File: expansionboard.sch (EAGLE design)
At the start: 40 parts, among them IC2 REG1117, IC3 REG1117, U1 LAN951X, X1 J1012F21R, Y1 20Mhz

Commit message: for now, a complete logic board and expansion board until I find something wrong with it
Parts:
- added C12, C13: (no value), SparkFun-Capacitors:CAPEZ
- added C14, C15, C19, C20: 0.1uf, SparkFun-Capacitors:CAP1206
- added C18: 4.7uf, SparkFun-Capacitors:CAP1206
- added JP1: USB-A-S, SparkFun-Connectors:USB-A-S
- added R8: (no value), SparkFun-Resistors:RESISTOR1206
- added R9: 0ohm, SparkFun-Resistors:RESISTOR1206
- added X2, X3, X4: PCI-60-POS-145167, con-amp:PCI-60-POS-145167
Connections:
- removed net 3.3V_AN: R1.2, R2.2, R3.2, R4.2
- new net N$27: U1_USB0.CLK24_OUT
- new net USB2+: U1_USB0.USB_DP2_P, X2-1.1, X2-2.1
- new net USB2-: U1_USB0.USB_DM2_N, X2-3.1, X2-4.1
- new net USB2_PWR: U1_USB0.PRTCTRL2, X2-5.1, X2-6.1
- new net USB3+: U1_USB0.USB_DP3_P, X3-1.1, X3-2.1
- new net USB3-: U1_USB0.USB_DM3_N, X3-3.1, X3-4.1
- new net USB3_PWR: U1_USB0.PRTCTRL3, X3-5.1, X3-6.1
- new net USB4+: U1_USB1.USB_DP4_P, X4-1.1, X4-2.1
- new net USB4-: U1_USB1.USB_DM4_N, X4-3.1, X4-4.1
- new net USB4_PWR: U1_USB1.PRTCTRL4, X4-5.1, X4-6.1
- new net USB5+: JP1.D+, U1_USB1.USB_DP5_P
- new net USB5-: JP1.D-, U1_USB1.USB_DM5_N
- new net USB5_PWR: JP1.VBUS, U1_USB1.PRTCTRL5
- new net VBUS_DET: R8.1, U1_USB0.VBUS_DET
- new net VDD18CORE: C18.1, C19.1, C20.1, U1_PWR.VDD_1V8_CORE1, U1_PWR.VDD_1V8_CORE2
- new net VDDA33: C14.1, C15.1, R1.2, R2.2, R3.2, R4.2, R9.2
- net 3.3V: now also C12.1, C13.1, R8.2, R9.1, U1_PWR.VDD_3V3_A1, U1_PWR.VDD_3V3_A2, U1_PWR.VDD_3V3_A3, U1_PWR.VDD_3V3_A4, U1_PWR.VDD_3V3_A5, U1_PWR.VDD_3V3_A6, U1_PWR.VDD_3V3_A7, U1_PWR.VDD_3V3_IO1, U1_PWR.VDD_3V3_IO2, U1_PWR.VDD_3V3_IO3, U1_PWR.VDD_3V3_IO4, U1_PWR.VDD_3V3_IO5
- net 5V: now also X2-13.1, X2-14.1, X2-15.1, X2-16.1, X2-17.1, X2-18.1, X3-13.1, X3-14.1, X3-15.1, X3-16.1, X3-17.1, X3-18.1, X4-13.1, X4-14.1, X4-15.1, X4-16.1, X4-17.1, X4-18.1
- net GND: now also C12.2, C13.2, C14.2, C15.2, C18.2, C19.2, C20.2, JP1.GND, X2-10.1, X2-11.1, X2-115.1, X2-116.1, X2-117.1, X2-118.1, X2-119.1, X2-12.1, X2-120.1, X2-7.1, X2-8.1, X2-9.1, X3-10.1, X3-11.1, X3-115.1, X3-116.1, X3-117.1, X3-118.1, X3-119.1, X3-12.1, X3-120.1, X3-7.1, X3-8.1, X3-9.1, X4-10.1, X4-11.1, X4-115.1, X4-116.1, X4-117.1, X4-118.1, X4-119.1, X4-12.1, X4-120.1, X4-7.1, X4-8.1, X4-9.1
- net GPIO10: now also X2-45.1, X2-46.1, X3-45.1, X3-46.1, X4-45.1, X4-46.1
- net GPIO11: now also X2-47.1, X2-48.1, X3-47.1, X3-48.1, X4-47.1, X4-48.1
- net GPIO12: now also X2-49.1, X2-50.1, X3-49.1, X3-50.1, X4-49.1, X4-50.1
- net GPIO13: now also X2-51.1, X2-52.1, X3-51.1, X3-52.1, X4-51.1, X4-52.1
- net GPIO17: now also X2-57.1, X2-58.1, X3-57.1, X3-58.1, X4-57.1, X4-58.1
- net GPIO18: now also X2-59.1, X2-60.1, X3-59.1, X3-60.1, X4-59.1, X4-60.1
- net GPIO19: now also X2-61.1, X2-62.1, X3-61.1, X3-62.1, X4-61.1, X4-62.1
- net GPIO20: now also X2-63.1, X2-64.1, X3-63.1, X3-64.1, X4-63.1, X4-64.1
- net GPIO21: now also X2-65.1, X2-66.1, X3-65.1, X3-66.1, X4-65.1, X4-66.1
- net GPIO22: now also X2-67.1, X2-68.1, X3-67.1, X3-68.1, X4-67.1, X4-68.1
- net GPIO23: now also X2-69.1, X2-70.1, X3-69.1, X3-70.1, X4-69.1, X4-70.1
- net GPIO24: now also X2-71.1, X2-72.1, X3-71.1, X3-72.1, X4-71.1, X4-72.1
- net GPIO25: now also X2-73.1, X2-74.1, X3-73.1, X3-74.1, X4-73.1, X4-74.1
- net GPIO26: now also X2-75.1, X2-76.1, X3-75.1, X3-76.1, X4-75.1, X4-76.1
- net GPIO27: now also X2-77.1, X2-78.1, X3-77.1, X3-78.1, X4-77.1, X4-78.1
- net GPIO28: now also X2-79.1, X2-80.1, X3-79.1, X3-80.1, X4-79.1, X4-80.1
- net GPIO29: now also X2-81.1, X2-82.1, X3-81.1, X3-82.1, X4-81.1, X4-82.1
- net GPIO30: now also X2-83.1, X2-84.1, X3-83.1, X3-84.1, X4-83.1, X4-84.1
- net GPIO31: now also X2-85.1, X2-86.1, X3-85.1, X3-86.1, X4-85.1, X4-86.1
- net GPIO32: now also X2-87.1, X2-88.1, X3-87.1, X3-88.1, X4-87.1, X4-88.1
- net GPIO33: now also X2-89.1, X2-90.1, X3-89.1, X3-90.1, X4-89.1, X4-90.1
- net GPIO34: now also X2-91.1, X2-92.1, X3-91.1, X3-92.1, X4-91.1, X4-92.1
- net GPIO35: now also X2-93.1, X2-94.1, X3-93.1, X3-94.1, X4-93.1, X4-94.1
- net GPIO36: now also X2-95.1, X2-96.1, X3-95.1, X3-96.1, X4-95.1, X4-96.1
- net GPIO37: now also X2-97.1, X2-98.1, X3-97.1, X3-98.1, X4-97.1, X4-98.1
- net GPIO38: now also X2-100.1, X2-99.1, X3-100.1, X3-99.1, X4-100.1, X4-99.1
- net GPIO39: now also X2-101.1, X2-102.1, X3-101.1, X3-102.1, X4-101.1, X4-102.1
- net GPIO4: now also X2-33.1, X2-34.1, X3-33.1, X3-34.1, X4-33.1, X4-34.1
- net GPIO40: now also X2-103.1, X2-104.1, X3-103.1, X3-104.1, X4-103.1, X4-104.1
- net GPIO41: now also X2-105.1, X2-106.1, X3-105.1, X3-106.1, X4-105.1, X4-106.1
- net GPIO42: now also X2-107.1, X2-108.1, X3-107.1, X3-108.1, X4-107.1, X4-108.1
- net GPIO43: now also X2-109.1, X2-110.1, X3-109.1, X3-110.1, X4-109.1, X4-110.1
- net GPIO44: now also X2-111.1, X2-112.1, X3-111.1, X3-112.1, X4-111.1, X4-112.1
- net GPIO45: now also X2-113.1, X2-114.1, X3-113.1, X3-114.1, X4-113.1, X4-114.1
- net GPIO5: now also X2-35.1, X2-36.1, X3-35.1, X3-36.1, X4-35.1, X4-36.1
- net GPIO6: now also X2-37.1, X2-38.1, X3-37.1, X3-38.1, X4-37.1, X4-38.1
- net GPIO7: now also X2-39.1, X2-40.1, X3-39.1, X3-40.1, X4-39.1, X4-40.1
- net GPIO8: now also X2-41.1, X2-42.1, X3-41.1, X3-42.1, X4-41.1, X4-42.1
- net GPIO9: now also X2-43.1, X2-44.1, X3-43.1, X3-44.1, X4-43.1, X4-44.1
- net RXD0: now also X2-55.1, X2-56.1, X3-55.1, X3-56.1, X4-55.1, X4-56.1
- net SCL: now also X2-27.1, X2-28.1, X3-27.1, X3-28.1, X4-27.1, X4-28.1
- net SCL1: now also X2-31.1, X2-32.1, X3-31.1, X3-32.1, X4-31.1, X4-32.1
- net SDA: now also X2-25.1, X2-26.1, X3-25.1, X3-26.1, X4-25.1, X4-26.1
- net SDA1: now also X2-29.1, X2-30.1, X3-29.1, X3-30.1, X4-29.1, X4-30.1
- net TXD0: now also X2-53.1, X2-54.1, X3-53.1, X3-54.1, X4-53.1, X4-54.1
- net USB+: now also U1_USB0.USB_DP0_P
- net USB-: now also U1_USB0.USB_DM0_N
- net V+: now also X2-19.1, X2-20.1, X2-21.1, X2-22.1, X2-23.1, X2-24.1, X3-19.1, X3-20.1, X3-21.1, X3-22.1, X3-23.1, X3-24.1, X4-19.1, X4-20.1, X4-21.1, X4-22.1, X4-23.1, X4-24.1

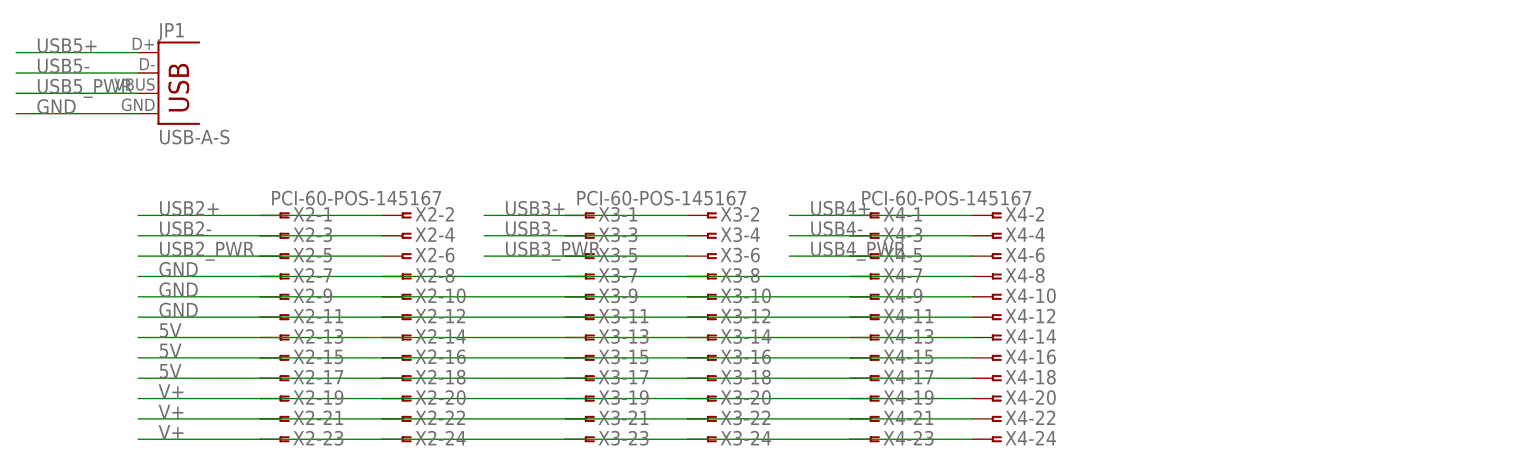
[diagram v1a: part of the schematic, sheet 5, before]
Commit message: Adding borders to schematics
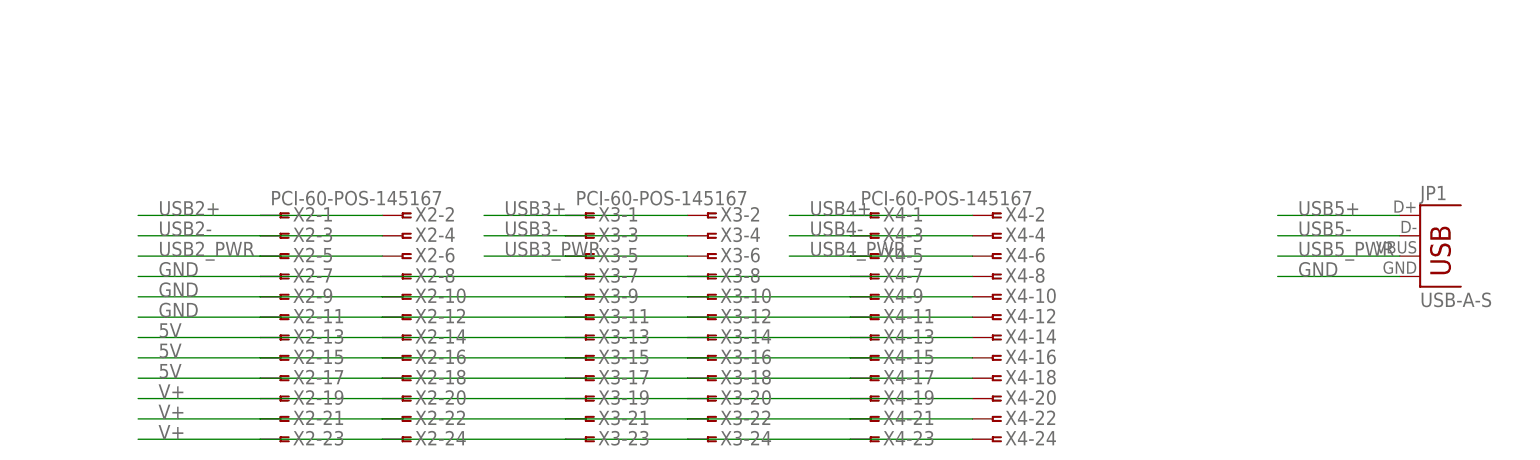
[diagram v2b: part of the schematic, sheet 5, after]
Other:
- moved on the sheet: JP1
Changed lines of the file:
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@@
 <part name="SUPPLY7" library="SparkFun-Aesthetics" deviceset="3.3V" device=""/>
 <part name="R9" library="SparkFun-Resistors" deviceset="RESISTOR" device="1206" value="0ohm"/>
+<part name="FRAME3" library="SparkFun-Aesthetics" deviceset="FRAME-A4L" device=""/>
+<part name="FRAME4" library="SparkFun-Aesthetics" deviceset="FRAME-A4L" device=""/>
+<part name="FRAME5" library="SparkFun-Aesthetics" deviceset="FRAME-A4L" device=""/>
+<part name="FRAME6" library="SparkFun-Aesthetics" deviceset="FRAME-A4L" device=""/>
 </parts>
 <sheets>
@@
 <instance part="H7" gate="G$1" x="203.2" y="215.9"/>
 <instance part="H8" gate="G$1" x="213.36" y="215.9"/>
+<instance part="FRAME3" gate="G$1" x="170.18" y="60.96"/>
 </instances>
 <busses>
@@
 <instance part="C4" gate="G$1" x="76.2" y="96.52"/>
 <instance part="C5" gate="G$1" x="83.82" y="96.52"/>
+<instance part="FRAME4" gate="G$1" x="-15.24" y="-15.24"/>
 </instances>
 <busses>
@@
 <instance part="GND1" gate="1" x="38.1" y="0"/>
 <instance part="GND28" gate="1" x="86.36" y="0"/>
+<instance part="FRAME5" gate="G$1" x="7.62" y="-45.72"/>
 </instances>
 <busses>
@@
 <instance part="X4" gate="-119" x="116.84" y="-60.96"/>
 <instance part="X4" gate="-120" x="132.08" y="-60.96"/>
-<instance part="JP1" gate="G$1" x="27.94" y="104.14"/>
+<instance part="JP1" gate="G$1" x="185.42" y="83.82"/>
+<instance part="FRAME6" gate="G$1" x="7.62" y="-78.74"/>
 </instances>
 <busses>
@@
 <segment>
 <pinref part="JP1" gate="G$1" pin="D+"/>
-<wire x1="25.4" y1="111.76" x2="10.16" y2="111.76" width="0.1524" layer="91"/>
-<label x="12.7" y="111.76" size="1.778" layer="95"/>
+<wire x1="182.88" y1="91.44" x2="167.64" y2="91.44" width="0.1524" layer="91"/>
+<label x="170.18" y="91.44" size="1.778" layer="95"/>
 </segment>
 </net>
@@
 <segment>
 <pinref part="JP1" gate="G$1" pin="D-"/>
-<wire x1="10.16" y1="109.22" x2="25.4" y2="109.22" width="0.1524" layer="91"/>
-<label x="12.7" y="109.22" size="1.778" layer="95"/>
+<wire x1="167.64" y1="88.9" x2="182.88" y2="88.9" width="0.1524" layer="91"/>
+<label x="170.18" y="88.9" size="1.778" layer="95"/>
 </segment>
 </net>
@@
 <segment>
 <pinref part="JP1" gate="G$1" pin="VBUS"/>
-<wire x1="25.4" y1="106.68" x2="10.16" y2="106.68" width="0.1524" layer="91"/>
-<label x="12.7" y="106.68" size="1.778" layer="95"/>
+<wire x1="182.88" y1="86.36" x2="167.64" y2="86.36" width="0.1524" layer="91"/>
+<label x="170.18" y="86.36" size="1.778" layer="95"/>
 </segment>
 </net>
@@
 <segment>
 <pinref part="JP1" gate="G$1" pin="GND"/>
-<wire x1="10.16" y1="104.14" x2="25.4" y2="104.14" width="0.1524" layer="91"/>
-<label x="12.7" y="104.14" size="1.778" layer="95"/>
-</segment>
-<segment>
+<wire x1="167.64" y1="83.82" x2="182.88" y2="83.82" width="0.1524" layer="91"/>
+<label x="170.18" y="83.82" size="1.778" layer="95"/>
+</segment>
+<segment>
